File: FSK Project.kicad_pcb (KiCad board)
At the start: 2 copper layers, 85.5 x 62 mm, 53 parts, among them J1 DATA IN, J2 TX_PAIR, J3 RX_PAIR, J4 DATA_OUT, Q1 2N3904, Q2 2N3904, SW1 MAN, U1 MC14046BCP, U2 LM393, U3 MC14046BCP

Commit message: Add page 5 filter information
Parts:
- added R19: 0R, Resistor_THT:R_Axial_DIN0204_L3.6mm_D1.6mm_P7.62mm_Horizontal, F.Cu at (180.5, 107.2)
- moved C4 5.00 mm to (177.0, 113.5), turned to 180 degrees
- moved TP5 4.12 mm to (167.5, 114.0)
- moved TP4 3.04 mm to (184.5, 105.5)
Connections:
- C4 pad 1: /DEM_OUT -> Net-(C4-Pad1)
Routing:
- net Net-(C4-Pad1): track 0.00 -> 7.76 mm
- net /DEM_OUT: track 47.8 -> 51.5 mm
- net Net-(U3-PC1): track 27.6 -> 31.2 mm
- net Net-(U3-SFout): track 4.67 -> 7.87 mm

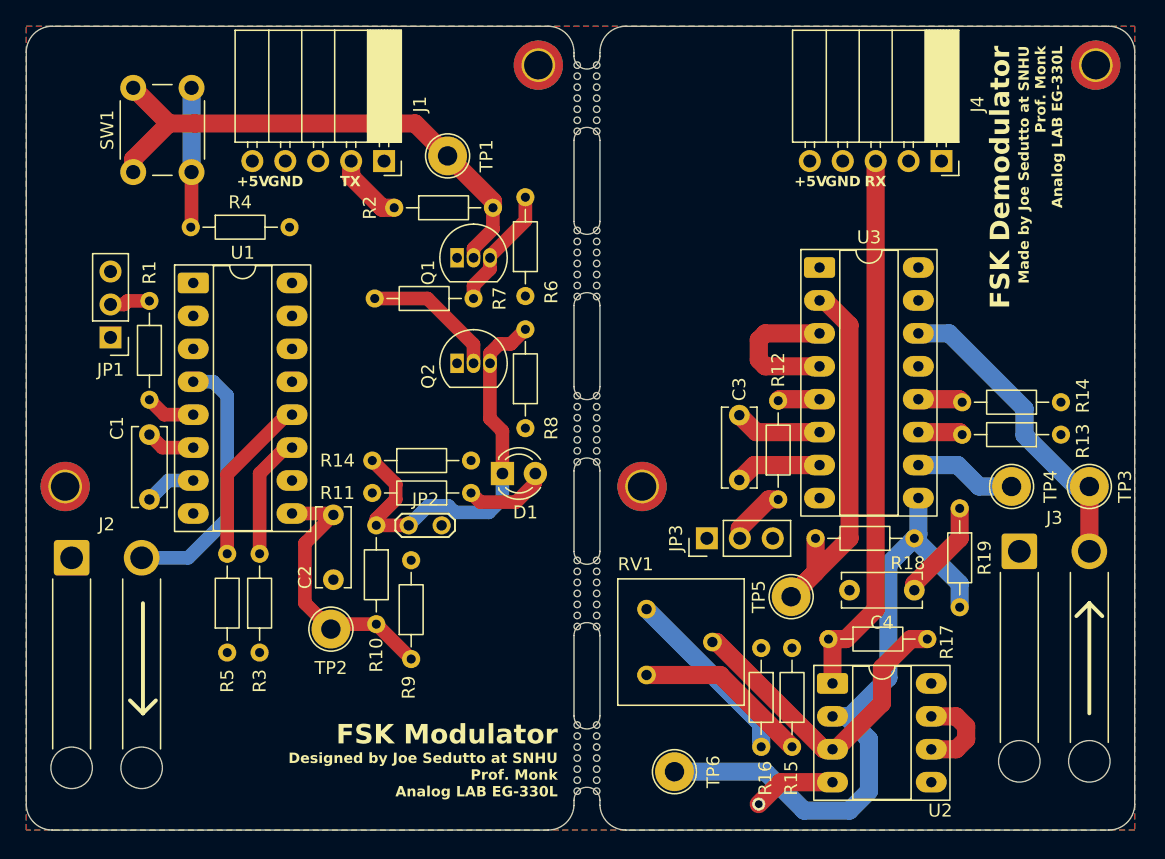
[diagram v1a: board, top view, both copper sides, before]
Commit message: Add static protection
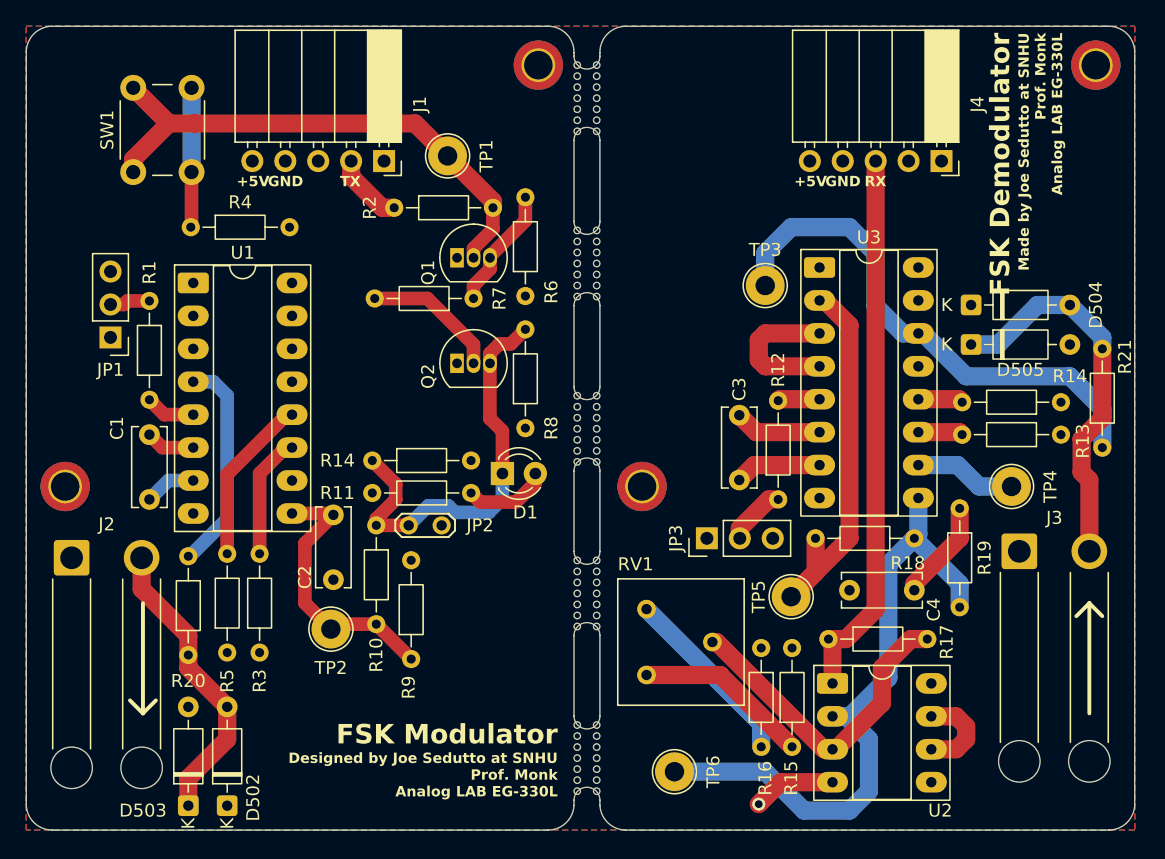
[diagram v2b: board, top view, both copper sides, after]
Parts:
- added D502: 1N4148, Diode_THT:D_DO-35_SOD27_P7.62mm_Horizontal, F.Cu at (124.0, 130.1)
- added D503: 1N4148, Diode_THT:D_DO-35_SOD27_P7.62mm_Horizontal, F.Cu at (121.0, 130.1)
- added D504: 1N4148, Diode_THT:D_DO-35_SOD27_P7.62mm_Horizontal, F.Cu at (181.4, 91.5)
- added D505: 1N4148, Diode_THT:D_DO-35_SOD27_P7.62mm_Horizontal, F.Cu at (181.4, 94.5)
- added R20: 100R, Resistor_THT:R_Axial_DIN0204_L3.6mm_D1.6mm_P7.62mm_Horizontal, F.Cu at (121.0, 118.5)
- added R21: 100R, Resistor_THT:R_Axial_DIN0204_L3.6mm_D1.6mm_P7.62mm_Horizontal, F.Cu at (191.5, 102.5)
- moved TP3 29.4 mm to (165.5, 90.0), turned to 90 degrees
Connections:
- J2 pad 2: /MOD_OUT -> Net-(D502-A)
- J3 pad 2: /MOD_IN -> Net-(D504-A)
- TP3 pad 1: /MOD_IN -> Net-(U3-SigIn)
- U3 pad 14: /MOD_IN -> Net-(U3-SigIn)
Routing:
- net Net-(U3-SigIn): track 0.00 -> 40.5 mm
- net Net-(D504-A): track 0.00 -> 29.8 mm
- net /MOD_IN: track 24.3 -> 0.00 mm
- net Net-(D502-A): track 0.00 -> 23.1 mm
- net /MOD_OUT: track 20.4 -> 16.8 mm
